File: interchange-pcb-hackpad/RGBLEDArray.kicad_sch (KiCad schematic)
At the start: 60 parts

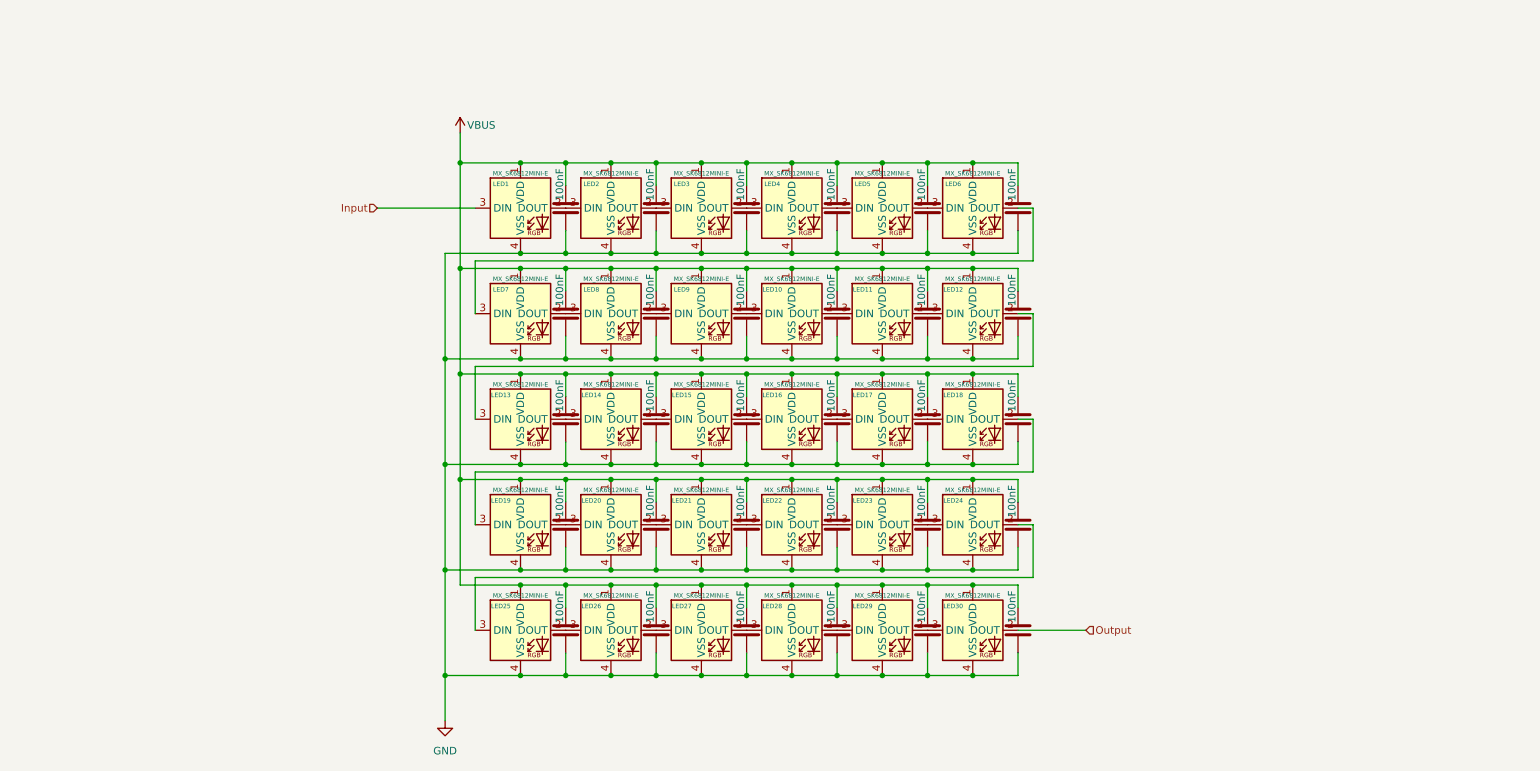
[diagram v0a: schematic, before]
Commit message: feat: create schematic for interchange-pcb-hackpad
and fix minor spacing issues with capaicitors in interchange-pcb-right
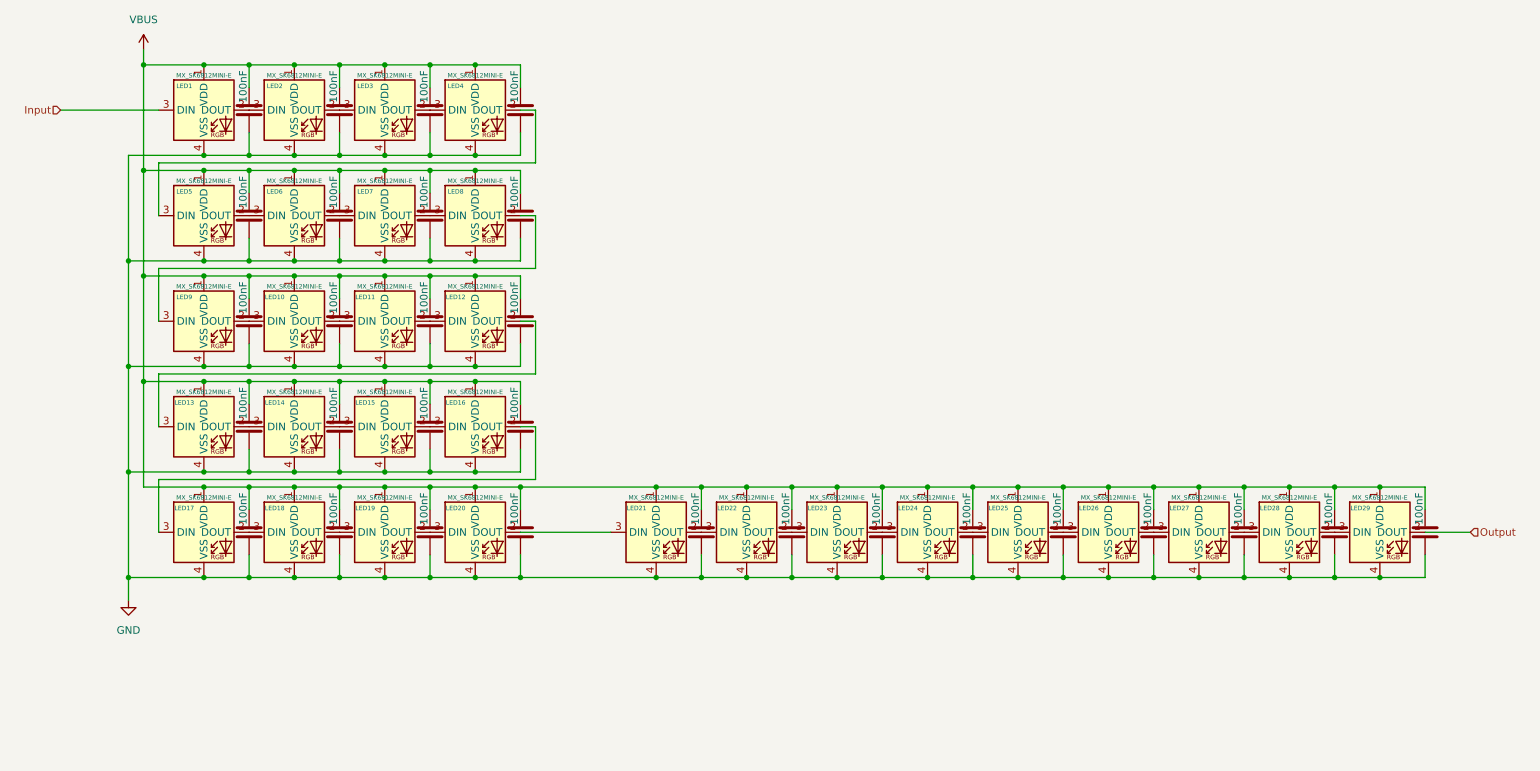
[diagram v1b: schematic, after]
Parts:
- removed C30: 100nF, Capacitor_SMD:C_0603_1608Metric_Pad1.08x0.95mm_HandSolder, symbol Device:C
- removed LED30: MX_SK6812MINI-E, CustomFootprints:LED_MX_6028R-ROT_Custom, symbol PCM_marbastlib-mx:MX_SK6812MINI-E
- LED21, LED22, LED23, LED24, LED25, LED26, LED27, LED28, LED29: footprint CustomFootprints:LED_MX_6028R-ROT_Custom -> CustomFootprints:LED_6028R_Custom
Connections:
- net Output: now also LED29.2 (DOUT)
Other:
- title: The Interchange Keyboard - Right Module -> The Interchange Keyboard - Hackpad Module
- moved on the sheet: LED1
